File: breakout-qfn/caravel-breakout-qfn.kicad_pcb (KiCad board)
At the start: 2 copper layers, 45 x 52.5 mm, 95 parts, among them CON1 REF-182665-01, CON2 REF-182665-01, U1 Caravel_QFN_TT4

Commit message: Comments and cleanup
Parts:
- added STITCH1: StitchingVia-0.3mm, flyingcarsfootprints:StitchingVia-0.3mm, F.Cu at (81.9, 20.6)
- added STITCH17: StitchingVia-0.3mm, flyingcarsfootprints:StitchingVia-0.3mm, F.Cu at (83.2, 46.9)
- moved STITCH1 0.79 mm to (82.7, 22.2)
- moved STITCH17 0.55 mm to (57.1, 58.6)
- moved STITCH17 0.55 mm to (62.6, 58.6)
- moved STITCH17 0.52 mm to (61.9, 42.9)
- moved C1 0.50 mm to (76.5, 47.0)
- moved C10 0.50 mm to (73.9, 48.6)
- moved C11 0.50 mm to (76.4, 36.6)
- moved C2 0.50 mm to (70.0, 48.8)
- moved C3 0.50 mm to (63.5, 45.0)
- moved C4 0.50 mm to (64.0, 38.8)
- moved C5 0.50 mm to (70.2, 35.2)
- moved C6 0.50 mm to (64.5, 37.0)
- moved C7 0.50 mm to (76.9, 38.3)
- moved CON1 0.50 mm to (52.5, 44.0)
- moved CON2 0.50 mm to (88.5, 44.0)
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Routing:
- net vddio: track 72.3 -> 70.3 mm

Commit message: aisler bridge markers
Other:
- board size 45 x 52.5 mm -> 45 x 57.6 mm
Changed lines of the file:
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@@
   (gr_line (start 72 67.5) (end 69 67.5)
     (stroke (width 0.05) (type solid)) (layer "Edge.Cuts"))
+  (gr_line (start 52.5 70) (end 52.5 72.5)
+    (stroke (width 0.05588) (type default)) (layer "Edge.Cuts"))
   (gr_arc locked (start 91 17.5) (mid 92.414214 18.085786) (end 93 19.5)
     (stroke (width 0.05) (type default)) (layer "Edge.Cuts"))
+  (gr_line (start 88.5 70.05) (end 88.5 72.55)
+    (stroke (width 0.05588) (type default)) (layer "Edge.Cuts"))
+  (gr_line (start 52.5 15) (end 52.5 17.5)
+    (stroke (width 0.05588) (type default)) (layer "Edge.Cuts"))
   (gr_arc (start 72 67.5) (mid 72.707107 67.792893) (end 73 68.5)
     (stroke (width 0.05) (type default)) (layer "Edge.Cuts"))
@@
   (gr_line (start 50 70) (end 67 70)
     (stroke (width 0.05) (type solid)) (layer "Edge.Cuts"))
+  (gr_line (start 88.5 14.95) (end 88.5 17.45)
+    (stroke (width 0.05588) (type default)) (layer "Edge.Cuts"))
   (gr_line locked (start 48 68) (end 48 19.5)
     (stroke (width 0.05) (type solid)) (layer "Edge.Cuts"))
@@
   (gr_line (start 91 70) (end 74 70)
     (stroke (width 0.05) (type solid)) (layer "Edge.Cuts"))
-  (gr_line (start 52.5 70) (end 52.5 72.5)
-    (stroke (width 0.05588) (type default)) (layer "Margin"))
-  (gr_line (start 88.5 70.05) (end 88.5 72.55)
-    (stroke (width 0.05588) (type default)) (layer "Margin"))
-  (gr_line (start 52.5 15) (end 52.5 17.5)
-    (stroke (width 0.05588) (type default)) (layer "Margin"))
-  (gr_line (start 88.5 14.95) (end 88.5 17.45)
-    (stroke (width 0.05588) (type default)) (layer "Margin"))
   (gr_text "(this side down)" (at 70.65 66.1) (layer "B.SilkS")
     (effects (font (size 2.5 2) (thickness 0.4)) (justify mirror))

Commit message: Added deglitch/delay on Caravel nRST
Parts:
- added C8: C_1u_0603_50V, Capacitor_SMD:C_0603_1608Metric, F.Cu at (59.5, 31.1)
- moved STITCH17 0.11 mm to (62.7, 34.1)
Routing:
- net ~{RST}: track 14.0 -> 19.7 mm, vias 0 -> 2
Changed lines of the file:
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@@
   )
   (footprint "flyingcarsfootprints:StitchingVia-0.3mm" (layer "F.Cu")
-    (at 62.6 34.1)
+    (at 62.7 34.15)
     (tags "stitching via")
     (attr through_hole board_only exclude_from_pos_files exclude_from_bom)
@@
       (net 1 "GND") (zone_connect 2))
   )
+  (footprint "Capacitor_SMD:C_0603_1608Metric" (layer "F.Cu")
+    (at 59.5 31.1 135)
+    (descr "Capacitor SMD 0603 (1608 Metric), square (rectangular) end terminal, IPC_7351 nominal, (Body size source: IPC-SM-782 page 76, https://www.pcb-3d.com/wordpress/wp-content/uploads/ipc-sm-782a_amendment_1_and_2.pdf), generated with kicad-footprint-generator")
+    (tags "capacitor")
+    (property "Display Value" "1u/50V")
+    (property "Manufacturer" "GRT188R61H105KE13D")
+    (property "Sheetfile" "caravel-breakout-qfn.kicad_sch")
+    (property "Sheetname" "")
+    (property "Vendor" "490-12330-1-ND")
+    (property "ki_description" "Unpolarized capacitor")
+    (property "ki_keywords" "cap capacitor")
+    (attr smd)
+    (fp_text reference "C8" (at 0 -1.43 135) (layer "F.SilkS") hide
+        (effects (font (size 1 1) (thickness 0.15)))
+    )
+    (fp_text value "C_1u_0603_50V" (at 0 1.43 135) (layer "F.Fab")
+        (effects (font (size 1 1) (thickness 0.15)))
+    )
+    (fp_text user "${REFERENCE}" (at 0 0 135) (layer "F.Fab")
+        (effects (font (size 0.4 0.4) (thickness 0.06)))
+    )
+    (fp_line (start -0.14058 -0.51) (end 0.14058 -0.51)
+      (stroke (width 0.12) (type solid)) (layer "F.SilkS"))
+    (fp_line (start -0.14058 0.51) (end 0.14058 0.51)
+      (stroke (width 0.12) (type solid)) (layer "F.SilkS"))
+    (fp_line (start -1.48 -0.73) (end 1.48 -0.73)
+      (stroke (width 0.05) (type solid)) (layer "F.CrtYd"))
+    (fp_line (start -1.48 0.73) (end -1.48 -0.73)
+      (stroke (width 0.05) (type solid)) (layer "F.CrtYd"))
+    (fp_line (start 1.48 -0.73) (end 1.48 0.73)
+      (stroke (width 0.05) (type solid)) (layer "F.CrtYd"))
+    (fp_line (start 1.48 0.73) (end -1.48 0.73)
+      (stroke (width 0.05) (type solid)) (layer "F.CrtYd"))
+    (fp_line (start -0.8 -0.4) (end 0.8 -0.4)
+      (stroke (width 0.1) (type solid)) (layer "F.Fab"))
+    (fp_line (start -0.8 0.4) (end -0.8 -0.4)
+      (stroke (width 0.1) (type solid)) (layer "F.Fab"))
+    (fp_line (start 0.8 -0.4) (end 0.8 0.4)
+      (stroke (width 0.1) (type solid)) (layer "F.Fab"))
+    (fp_line (start 0.8 0.4) (end -0.8 0.4)
+      (stroke (width 0.1) (type solid)) (layer "F.Fab"))
+    (pad "1" smd roundrect (at -0.775 0 135) (size 0.9 0.95) (layers "F.Cu" "F.Paste" "F.Mask") (roundrect_rratio 0.25)
+      (net 44 "~{RST}") (pintype "passive"))
+    (pad "2" smd roundrect (at 0.775 0 135) (size 0.9 0.95) (layers "F.Cu" "F.Paste" "F.Mask") (roundrect_rratio 0.25)
+      (net 1 "GND") (pintype "passive"))
+    (model "${KICAD6_3DMODEL_DIR}/Capacitor_SMD.3dshapes/C_0603_1608Metric.wrl"
+      (offset (xyz 0 0 0))
+      (scale (xyz 1 1 1))
+      (rotate (xyz 0 0 0))
+    )
+  )
   (footprint "flyingcarsfootprints:StitchingVia-0.3mm" (layer "F.Cu")
     (at 62.6 49.5)
@@
   (segment (start 64.06005 40.45) (end 64.79114 40.45) (width 0.2) (layer "F.Cu") (net 44))
   (segment (start 64.99114 40.25) (end 66.05 40.25) (width 0.2) (layer "F.Cu") (net 44))
+  (segment (start 57.898008 31.648008) (end 57.15 30.9) (width 0.18) (layer "F.Cu") (net 44))
   (segment (start 55.35 32.57) (end 56.18005 32.57) (width 0.2) (layer "F.Cu") (net 44))
+  (segment (start 60.048008 31.648008) (end 57.898008 31.648008) (width 0.18) (layer "F.Cu") (net 44))
   (segment (start 64.79114 40.45) (end 64.99114 40.25) (width 0.2) (layer "F.Cu") (net 44))
+  (via (at 57.15 30.9) (size 0.7) (drill 0.3) (layers "F.Cu" "B.Cu") (net 44))
+  (via (at 56.830025 33.219975) (size 0.7) (drill 0.3) (layers "F.Cu" "B.Cu") (net 44))
+  (segment (start 57.15 30.9) (end 56.830025 31.219975) (width 0.18) (layer "B.Cu") (net 44))
+  (segment (start 56.830025 31.219975) (end 56.830025 33.219975) (width 0.18) (layer "B.Cu") (net 44))
   (segment (start 65.244996 43.37) (end 65.33965 43.275345) (width 0.2) (layer "F.Cu") (net 45))
   (segment (start 66.024655 43.275345) (end 66.05 43.25) (width 0.2) (layer "F.Cu") (net 45))
@@
   (segment (start 64.315395 45.055345) (end 64.41005 45.15) (width 0.2) (layer "F.Cu") (net 52))
   (segment (start 50.873776 43.59) (end 50.89 43.59) (width 0.2) (layer "F.Cu") (net 52))
+  (segment (start 49.941579 27.49) (end 54.051579 31.6) (width 0.2) (layer "F.Cu") (net 53))
   (segment (start 64.48 38.8) (end 66 38.8) (width 0.2) (layer "F.Cu") (net 53))
+  (segment (start 54.051579 31.6) (end 57.29149 31.6) (width 0.2) (layer "F.Cu") (net 53))
   (segment (start 66 38.8) (end 66.05 38.75) (width 0.2) (layer "F.Cu") (net 53))
-  (segment (start 53.751579 31.3) (end 56.99149 31.3) (width 0.2) (layer "F.Cu") (net 53))
   (segment (start 64.48 38.78851) (end 64.48 38.8) (width 0.2) (layer "F.Cu") (net 53))
-  (segment (start 56.99149 31.3) (end 64.48 38.78851) (width 0.2) (layer "F.Cu") (net 53))
+  (segment (start 57.29149 31.6) (end 64.48 38.78851) (width 0.2) (layer "F.Cu") (net 53))
   (segment (start 49.65 27.49) (end 49.941579 27.49) (width 0.2) (layer "F.Cu") (net 53))
-  (segment (start 49.941579 27.49) (end 53.751579 31.3) (width 0.2) (layer "F.Cu") (net 53))
   (zone (net 1) (net_name "GND") (layers "F&B.Cu") (hatch edge 0.5)
     (priority 1)

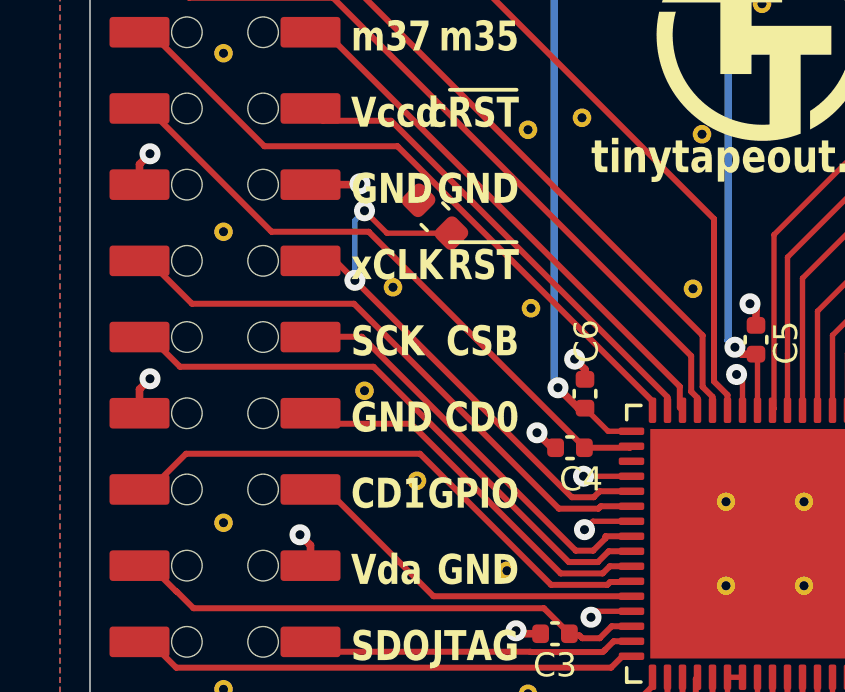
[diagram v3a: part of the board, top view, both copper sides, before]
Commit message: Silkscreen cleanup
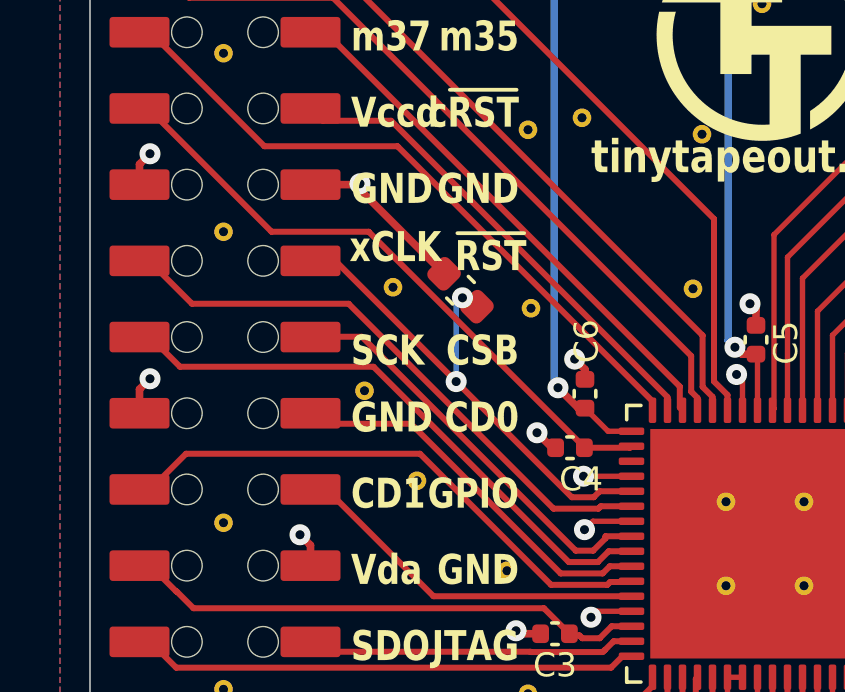
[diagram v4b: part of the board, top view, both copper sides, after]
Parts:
- moved C8 2.59 mm to (60.4, 33.5)
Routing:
- net GND: track 49.0 -> 53.2 mm
- net ~{RST}: track 19.7 -> 17.5 mm

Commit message: TT03p5, as fabbed
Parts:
- removed the REF** at (70.5, 65.8)
- removed the REF** at (70.5, 56.0)
- removed the REF** at (70.5, 61.8)
- added EFABLOG: Logo, Logos:ef_logo_graphical, F.Cu at (70.5, 53.8)
- added EFABTXT: Logo, Logos:ef_logo, F.Cu at (70.5, 58.1)
- added STITCH17: StitchingVia-0.3mm, flyingcarsfootprints:StitchingVia-0.3mm, F.Cu at (91.8, 26.2)
- added STITCH17: StitchingVia-0.3mm, flyingcarsfootprints:StitchingVia-0.3mm, F.Cu at (83.1, 27.3)
- added STITCH17: StitchingVia-0.3mm, flyingcarsfootprints:StitchingVia-0.3mm, F.Cu at (79.0, 25.7)
- added STITCH17: StitchingVia-0.3mm, flyingcarsfootprints:StitchingVia-0.3mm, F.Cu at (58.0, 43.4)
- moved G*** 3.85 mm to (70.7, 27.9)
- moved STITCH17 2.90 mm to (65.5, 49.5)
- moved REF** 2.55 mm to (70.4, 27.6)
- moved STITCH17 1.50 mm to (64.1, 47.0)
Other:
- board size 45 x 57.6 mm -> 45 x 52.5 mm
- board text added: "(C) 2024 Tiny Tapeout"
- board text added: "Pat Deegan"
- board text added: "QFN breakout"
- board text added: "TT RUN 3p5"
- board text added: "by Pat Deegan https://psychogenic.com"
- board text added: "for TT04+"
- board text added: "v3.1"
- board text removed: "(C) 2023 Pat Deegan"
- board text removed: "(C) 2023 Pat Deegan https://psychogenic.com"
- board text removed: "AISLER"
- board text removed: "Bridge markers |x4"
- board text removed: "Caravel QFN breakout"
- board text removed: "v3.0"

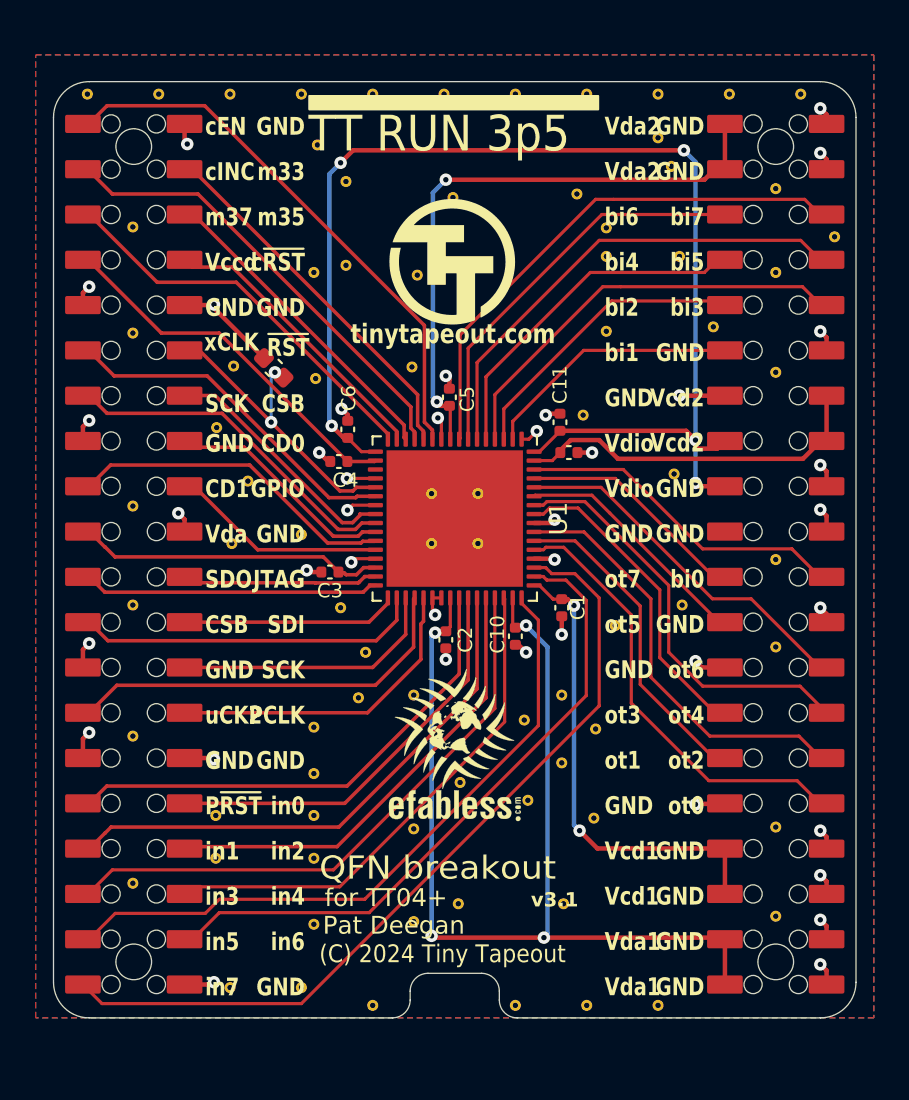
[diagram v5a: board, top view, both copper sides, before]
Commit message: v3.2 moved to bottom side pin headers
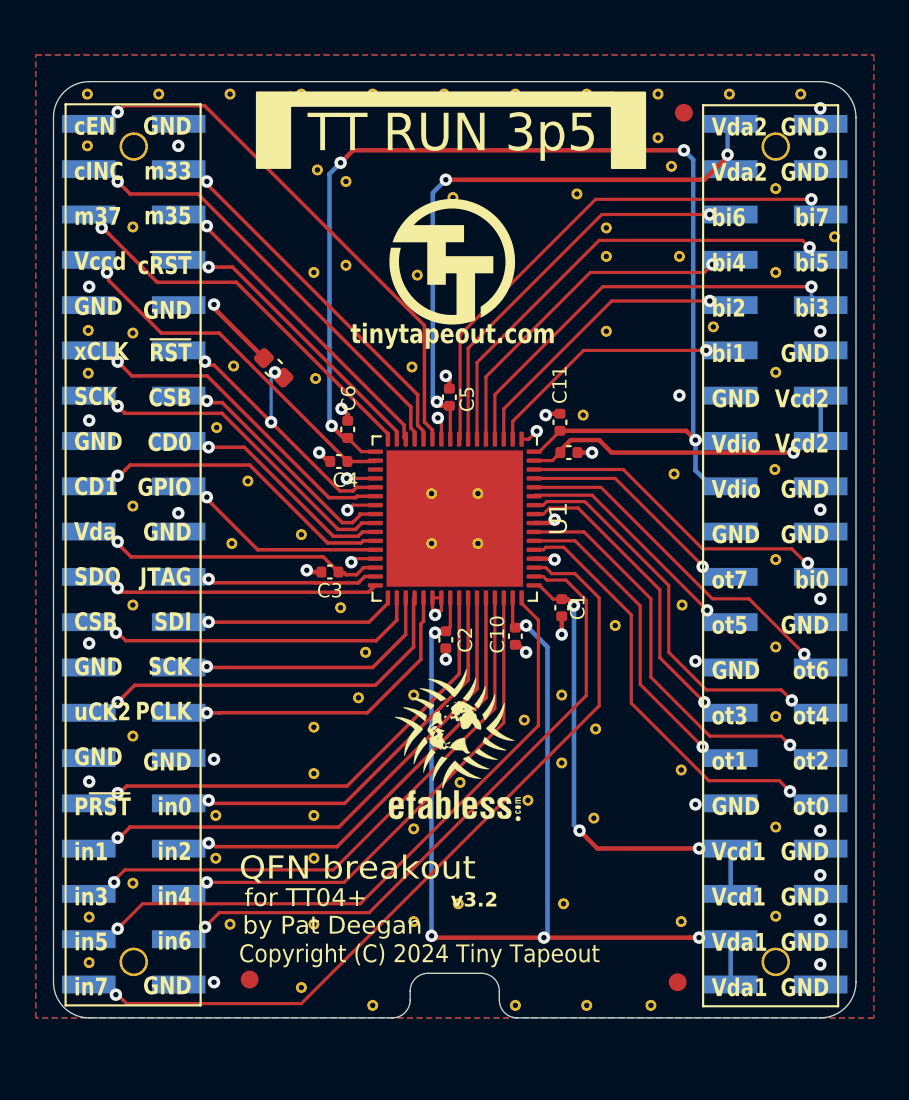
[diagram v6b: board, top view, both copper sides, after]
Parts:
- added FID1: Fiducial, Fiducial:Fiducial_1mm_Mask2mm, F.Cu at (59.0, 67.8)
- added FID2: Fiducial, Fiducial:Fiducial_1mm_Mask2mm, F.Cu at (83.3, 19.2)
- added FID3: Fiducial, Fiducial:Fiducial_1mm_Mask2mm, F.Cu at (83.0, 68.0)
- added STITCH17: StitchingVia-0.3mm, flyingcarsfootprints:StitchingVia-0.3mm, F.Cu at (49.9, 21.1)
- added STITCH17: StitchingVia-0.3mm, flyingcarsfootprints:StitchingVia-0.3mm, F.Cu at (88.5, 53.1)
- added STITCH17: StitchingVia-0.3mm, flyingcarsfootprints:StitchingVia-0.3mm, F.Cu at (50.0, 64.3)
- added STITCH17: StitchingVia-0.3mm, flyingcarsfootprints:StitchingVia-0.3mm, F.Cu at (83.2, 64.6)
- added STITCH17: StitchingVia-0.3mm, flyingcarsfootprints:StitchingVia-0.3mm, F.Cu at (50.0, 33.9)
- added STITCH17: StitchingVia-0.3mm, flyingcarsfootprints:StitchingVia-0.3mm, F.Cu at (50.0, 31.4)
- added STITCH17: StitchingVia-0.3mm, flyingcarsfootprints:StitchingVia-0.3mm, F.Cu at (83.2, 56.1)
- added STITCH17: StitchingVia-0.3mm, flyingcarsfootprints:StitchingVia-0.3mm, F.Cu at (88.5, 39.2)
- added STITCH17: StitchingVia-0.3mm, flyingcarsfootprints:StitchingVia-0.3mm, F.Cu at (50.0, 66.9)
- C8: value C_1u_0603_50V -> 1u
- CON1, CON2: value REF-182665-01 -> ~; footprint BreakoutCommon:FH-00339 -> TinyTapeout:FH-00148_PinSocket_2x20_P2.54mm; moved to B.Cu
- moved STITCH3 3.55 mm to (57.9, 64.8)
- moved STITCH17 1.40 mm to (62.8, 22.4)
- moved REF** 1.35 mm to (64.2, 60.0)
- moved REF** 1.35 mm to (78.8, 60.4)
- moved STITCH17 0.40 mm to (81.5, 69.3)
- turned CON1 to 180 degrees
- turned CON2 to 180 degrees
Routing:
- net GND: track 53.2 -> 24.0 mm, vias 39 -> 38
- net uio[1]/mio[25]: track 14.5 -> 13.5 mm, vias 0 -> 1
- net uio[2]/mio[26]: track 16.7 -> 15.8 mm, vias 0 -> 1
- net uio[6]/mio[30]: track 22.6 -> 21.8 mm, vias 0 -> 1
- net uio[4]/mio[28]: track 19.6 -> 18.8 mm, vias 0 -> 1
- net vdda2: track 34.0 -> 34.7 mm, vias 2 -> 3
- net uo_out[3]/mio[19]: track 17.8 -> 18.5 mm, vias 0 -> 1
- net vccd2: track 20.3 -> 19.7 mm, vias 0 -> 1
- net mio[33]: track 20.9 -> 21.5 mm, vias 0 -> 1
- net ui_in[6]/mio[14]: track 37.0 -> 37.5 mm, vias 0 -> 1
- net gpio: track 12.2 -> 12.7 mm, vias 0 -> 1
- net ui_in[2]/mio[10]: track 26.0 -> 26.5 mm, vias 0 -> 1
- net ui_in[0]/mio[8]: track 23.4 -> 23.8 mm, vias 0 -> 1
- net ~{RST}: track 17.5 -> 18.0 mm, vias 2 -> 3
- net mio[35]: track 18.0 -> 18.4 mm, vias 0 -> 1
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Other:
- board text added: "Copyright (C) 2024 Tiny Tapeout"
- board text added: "TT QFN breakout v3"
- board text added: "by Pat Deegan"
- board text added: "github.com/TinyTapeout/caravel-breakout-pcb"
- board text added: "v3.2"
- board text removed: "(C) 2024 Tiny Tapeout"
- board text removed: "(this side down)"
- board text removed: "Caravel QFN breakout v3"
- board text removed: "Pat Deegan"
- board text removed: "https://github.com/TinyTapeout/caravel-breakout-pcb"
- board text removed: "v3.1"
